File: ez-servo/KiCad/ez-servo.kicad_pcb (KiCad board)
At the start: 4 copper layers, 20 x 20 mm, 14 parts, among them J2 SERVO, J3 VSEL, U1 TPS5430DDA

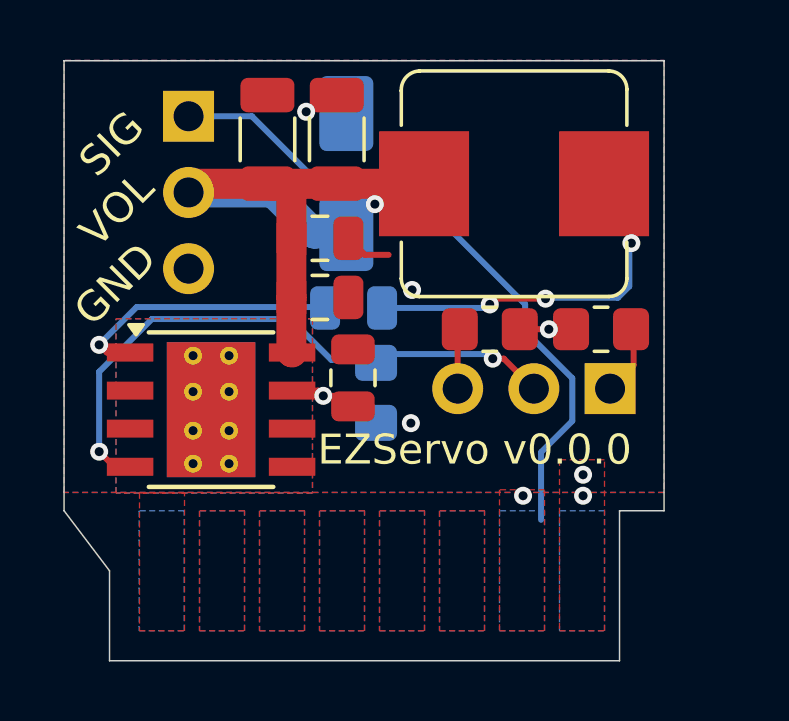
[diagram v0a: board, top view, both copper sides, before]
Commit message: feat: add optional servo output through stepper port
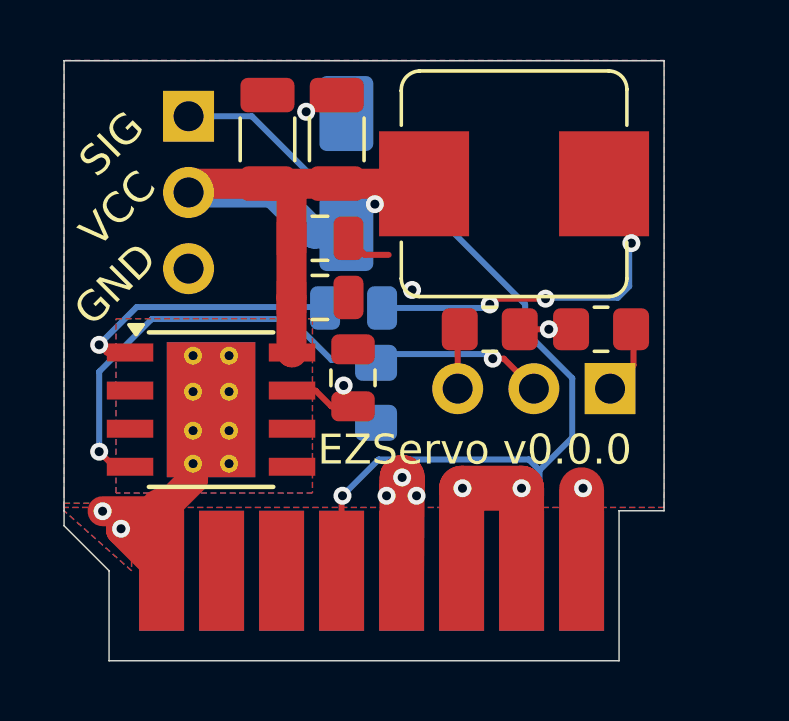
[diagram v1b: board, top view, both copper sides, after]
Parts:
- added J1: Driver Pins, Local Library:BTT EZ, B.Cu at (35.0, 42.0)
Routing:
- net GND: track 2.15 -> 19.5 mm, vias 4 -> 6
- net +24V: track 2.33 -> 14.4 mm, vias 3 -> 2
- net SERVO_PWM: track 22.1 -> 33.8 mm, vias 0 -> 1
- net VOUT: track 31.0 -> 34.7 mm, vias 2 -> 5
- added copper zone on In1.Cu, net VOUT
- removed copper zone on B.Cu, net (none)
- removed copper zone on F.Cu, net (none)
- removed copper zone on F.Cu, net +24V
- removed copper zone on In1.Cu, net +24V
- removed copper zone on B.Cu, net SERVO_PWM
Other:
- board size 20 x 20 mm -> 20 x 15 mm
- board text added: "VCC"
- board text removed: "VOL"
